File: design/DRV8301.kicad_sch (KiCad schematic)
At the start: 38 parts, among them U2 LM3671, U3 DRV8301

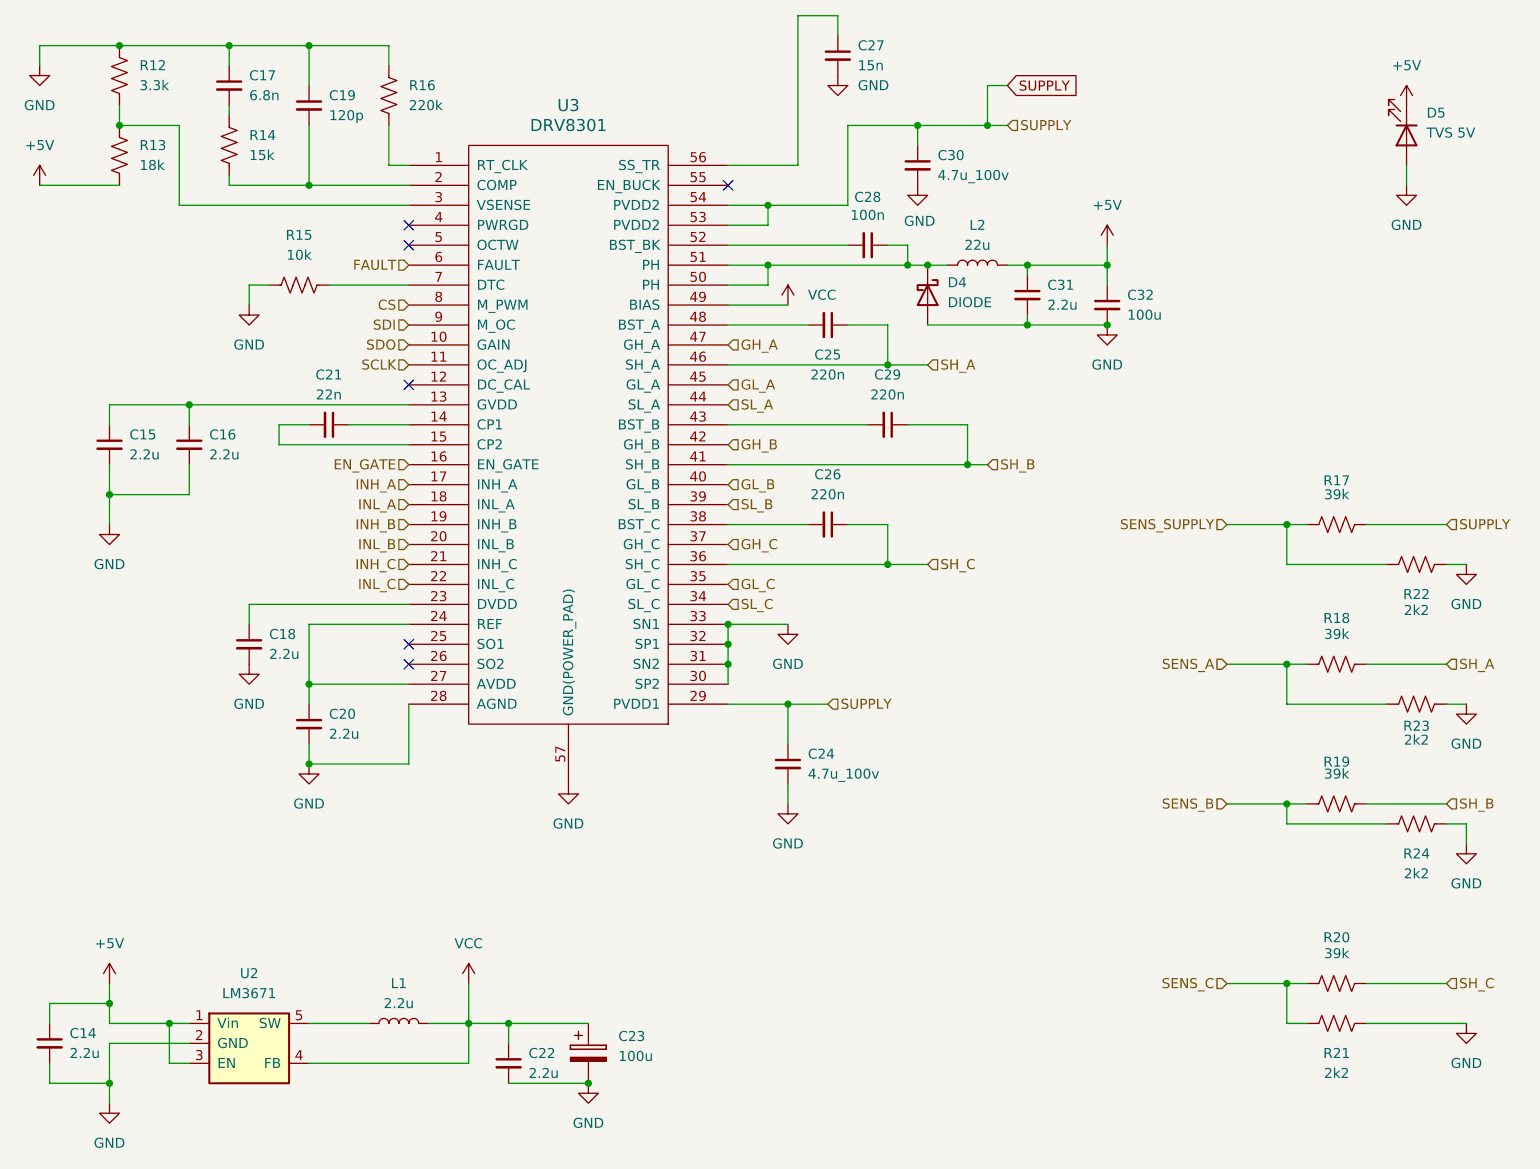
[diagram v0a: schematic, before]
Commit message: Impresión de esquemático en pdf
Impresión de la versión del esquemático en la carpeta /pdf
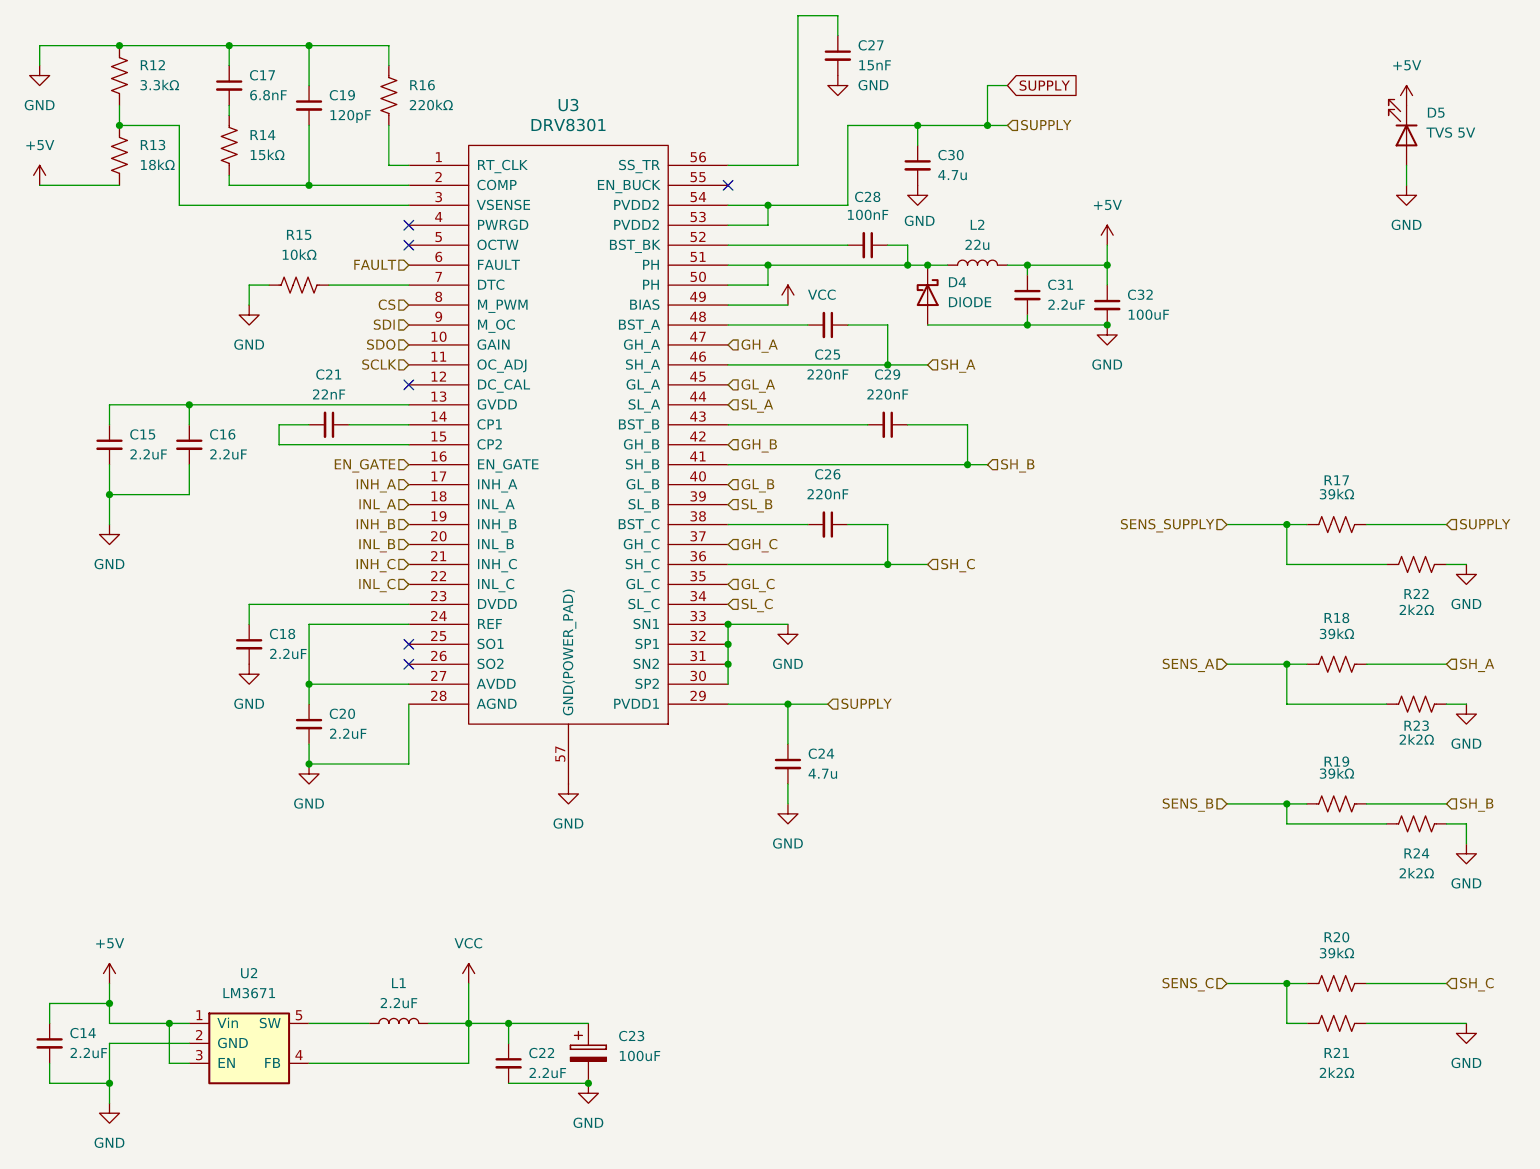
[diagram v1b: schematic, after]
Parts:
- C14, C15, C16, C18, C20, C22, C31, L1: value 2.2u -> 2.2uF
- C17: value 6.8n -> 6.8nF; footprint Capacitor_SMD:C_0603_1608Metric -> Capacitor_SMD:C_1206_3216Metric
- C19: value 120p -> 120pF
- C21: value 22n -> 22nF
- C23, C32: value 100u -> 100uF; footprint Capacitor_SMD:C_0603_1608Metric -> Capacitor_SMD:C_1206_3216Metric
- C24, C30: value 4.7u_100v -> 4.7u; footprint Capacitor_SMD:C_0603_1608Metric -> Capacitor_SMD:C_1210_3225Metric
- C25, C26, C29: value 220n -> 220nF
- C27: value 15n -> 15nF
- C28: value 100n -> 100nF
- R12: value 3.3k -> 3.3kΩ
- R13: value 18k -> 18kΩ
- R14: value 15k -> 15kΩ
- R15: value 10k -> 10kΩ
- R16: value 220k -> 220kΩ
- R17, R18, R19, R20: value 39k -> 39kΩ
- R21, R22, R23, R24: value 2k2 -> 2k2Ω
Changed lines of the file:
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@@
 			)
 		)
-		(property "Value" "220k"
+		(property "Value" "220kΩ"
 			(at 121.92 30.4799 0)
 			(effects
@@
 			)
 		)
-		(property "Value" "18k"
+		(property "Value" "18kΩ"
 			(at 87.63 38.0999 0)
 			(effects
@@
 			)
 		)
-		(property "Value" "3.3k"
+		(property "Value" "3.3kΩ"
 			(at 87.63 27.9399 0)
 			(effects
@@
 			)
 		)
-		(property "Value" "15k"
+		(property "Value" "15kΩ"
 			(at 101.6 36.8299 0)
 			(effects
@@
 			)
 		)
-		(property "Value" "6.8n"
+		(property "Value" "6.8nF"
 			(at 101.6 29.2162 0)
 			(effects
@@
 			)
 		)
-		(property "Footprint" "Capacitor_SMD:C_0603_1608Metric"
+		(property "Footprint" "Capacitor_SMD:C_1206_3216Metric"
 			(at 99.06 27.94 0)
 			(effects
@@
 			)
 		)
-		(property "Description" ""
+		(property "Description" "CAP CER 6.8NF 1206"
 			(at 99.06 27.94 0)
 			(effects
@@
 			)
 		)
-		(property "Value" "120p"
+		(property "Value" "120pF"
 			(at 111.76 31.7562 0)
 			(effects
@@
 			)
 		)
-		(property "Description" ""
+		(property "Description" "CAP CER 120PF 0603"
 			(at 109.22 30.48 0)
 			(effects
@@
 			)
 		)
-		(property "Value" "22n"
+		(property "Value" "22nF"
 			(at 111.7536 67.31 90)
 			(effects
@@
 			)
 		)
-		(property "Description" ""
+		(property "Description" "CAP CER 22NF 0603"
 			(at 111.76 71.12 0)
 			(effects
@@
 			)
 		)
-		(property "Value" "2.2u"
+		(property "Value" "2.2uF"
 			(at 96.52 74.9362 0)
 			(effects
@@
 			)
 		)
-		(property "Value" "2.2u"
+		(property "Value" "2.2uF"
 			(at 86.36 74.9362 0)
 			(effects
@@
 			)
 		)
-		(property "Value" "2.2u"
+		(property "Value" "2.2uF"
 			(at 104.14 100.3362 0)
 			(effects
@@
 			)
 		)
-		(property "Value" "2.2u"
+		(property "Value" "2.2uF"
 			(at 111.76 110.4962 0)
 			(effects
@@
 			)
 		)
-		(property "Value" "15n"
+		(property "Value" "15nF"
 			(at 179.07 25.4062 0)
 			(effects
@@
 			)
 		)
-		(property "Description" ""
+		(property "Description" "CAP CER 0603 15nF 16V X7R 10%"
 			(at 176.53 24.13 0)
 			(effects
@@
 			)
 		)
-		(property "Value" "4.7u_100v"
+		(property "Value" "4.7u"
 			(at 189.23 39.3762 0)
 			(effects
@@
 			)
 		)
-		(property "Footprint" "Capacitor_SMD:C_0603_1608Metric"
+		(property "Footprint" "Capacitor_SMD:C_1210_3225Metric"
 			(at 186.69 38.1 0)
 			(effects
@@
 			)
 		)
-		(property "Description" ""
+		(property "Description" "CAP CER 4.7UF 100V X7R 1210"
 			(at 186.69 38.1 0)
 			(effects
@@
 			)
 		)
-		(property "Value" "220n"
+		(property "Value" "220nF"
 			(at 175.2536 64.77 90)
 			(effects
@@
 			)
 		)
-		(property "Description" ""
+		(property "Description" "CAP CER 0603 220nF 25V X7R 10%"
 			(at 175.26 58.42 0)
 			(effects
@@
 			)
 		)
-		(property "Value" "100n"
+		(property "Value" "100nF"
 			(at 180.3336 44.45 90)
 			(effects
@@
 			)
 		)
-		(property "Value" "220n"
+		(property "Value" "220nF"
 			(at 182.8736 67.31 90)
 			(effects
@@
 			)
 		)
-		(property "Description" ""
+		(property "Description" "CAP CER 0603 220nF 25V X7R 10%"
 			(at 182.88 71.12 0)
 			(effects
@@
 			)
 		)
-		(property "Value" "220n"
+		(property "Value" "220nF"
 			(at 175.2536 80.01 90)
 			(effects
@@
 			)
 		)
-		(property "Description" ""
+		(property "Description" "CAP CER 0603 220nF 25V X7R 10%"
 			(at 175.26 83.82 0)
 			(effects
@@
 			)
 		)
-		(property "Value" "2.2u"
+		(property "Value" "2.2uF"
 			(at 203.2 55.8862 0)
 			(effects
@@
 			)
 		)
-		(property "Value" "100u"
+		(property "Value" "100uF"
 			(at 213.36 57.1562 0)
 			(effects
@@
 			)
 		)
-		(property "Footprint" "Capacitor_SMD:C_0603_1608Metric"
+		(property "Footprint" "Capacitor_SMD:C_1206_3216Metric"
 			(at 210.82 55.88 0)
 			(effects
@@
 			)
 		)
-		(property "Description" ""
+		(property "Description" "CAP CER 100UF 1206"
 			(at 210.82 55.88 0)
 			(effects
@@
 			)
 		)
-		(property "Value" "4.7u_100v"
+		(property "Value" "4.7u"
 			(at 172.72 115.5762 0)
 			(effects
@@
 			)
 		)
-		(property "Footprint" "Capacitor_SMD:C_0603_1608Metric"
+		(property "Footprint" "Capacitor_SMD:C_1210_3225Metric"
 			(at 170.18 114.3 0)
 			(effects
@@
 			)
 		)
-		(property "Description" ""
+		(property "Description" "CAP CER 4.7UF 100V X7R 1210"
 			(at 170.18 114.3 0)
 			(effects
@@
 			)
 		)
-		(property "Value" "39k"
+		(property "Value" "39kΩ"
 			(at 240.03 80.01 90)
 			(effects
@@
 			)
 		)
-		(property "Value" "2k2"
+		(property "Value" "2k2Ω"
 			(at 250.19 94.742 90)
 			(effects
@@
 			)
 		)
-		(property "Value" "39k"
+		(property "Value" "39kΩ"
 			(at 240.03 97.79 90)
 			(effects
@@
 			)
 		)
-		(property "Value" "2k2"
+		(property "Value" "2k2Ω"
 			(at 250.19 111.252 90)
 			(effects
@@
 			)
 		)
-		(property "Value" "39k"
+		(property "Value" "39kΩ"
 			(at 240.03 115.57 90)
 			(effects
@@
 			)
 		)
-		(property "Value" "2k2"
+		(property "Value" "2k2Ω"
 			(at 250.19 128.27 90)
 			(effects
@@
 			)
 		)
-		(property "Value" "39k"
+		(property "Value" "39kΩ"
 			(at 240.03 138.43 90)
 			(effects
@@
 			)
 		)
-		(property "Value" "2k2"
+		(property "Value" "2k2Ω"
 			(at 240.03 153.67 90)
 			(effects
@@
 			)
 		)
-		(property "Value" "10k"
+		(property "Value" "10kΩ"
 			(at 107.95 49.53 90)
 			(effects
@@
 			)
 		)
-		(property "Value" "2.2u"
+		(property "Value" "2.2uF"
 			(at 120.65 144.78 90)
 			(effects
@@
 			)
 		)
-		(property "Value" "2.2u"
+		(property "Value" "2.2uF"
 			(at 137.16 153.6762 0)
 			(effects
@@
 			)
 		)
-		(property "Value" "2.2u"
+		(property "Value" "2.2uF"
 			(at 78.74 151.1362 0)
 			(effects
@@
 			)
 		)
-		(property "Value" "100u"
+		(property "Value" "100uF"
 			(at 148.59 151.5109 0)
 			(effects
@@
 			)
 		)
-		(property "Footprint" "Capacitor_SMD:C_0603_1608Metric"
+		(property "Footprint" "Capacitor_SMD:C_1206_3216Metric"
 			(at 145.7452 154.94 0)
 			(effects
@@
 			)
 		)
-		(property "Description" ""
+		(property "Description" "CAP CER 100UF 1206"
 			(at 144.78 151.13 0)
 			(effects

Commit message: Agregado de footprints
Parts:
- D4: footprint (none) -> Diode_SMD:D_SMA
- D5: footprint (none) -> LED_SMD:LED_0603_1608Metric
- L2: footprint (none) -> Inductor_SMD:L_0603_1608Metric_Pad1.05x0.95mm_HandSolder
- U2: footprint (none) -> crf1:MF05A
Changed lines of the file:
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@@
 			)
 		)
-		(property "Footprint" ""
+		(property "Footprint" "LED_SMD:LED_0603_1608Metric"
 			(at 248.92 34.29 0)
 			(effects
@@
 			)
 		)
-		(property "Description" ""
+		(property "Description" "LED"
 			(at 248.92 34.29 0)
 			(effects
@@
 			)
 		)
-		(property "Description" "R 2k2, 0603 "
+		(property "Description" "R 2k2, 0603"
 			(at 250.19 88.9 0)
 			(effects
@@
 			)
 		)
-		(property "Description" "R 2k2, 0603 "
+		(property "Description" "R 2k2, 0603"
 			(at 250.19 106.68 0)
 			(effects
@@
 			)
 		)
-		(property "Description" "R 2k2, 0603 "
+		(property "Description" "R 2k2, 0603"
 			(at 250.19 121.92 0)
 			(effects
@@
 			)
 		)
-		(property "Description" "R 2k2, 0603 "
+		(property "Description" "R 2k2, 0603"
 			(at 240.03 147.32 0)
 			(effects
@@
 			)
 		)
-		(property "Footprint" ""
+		(property "Footprint" "Diode_SMD:D_SMA"
 			(at 187.96 54.61 0)
 			(effects
@@
 			)
 		)
-		(property "Description" "Shottky 60V 2A "
+		(property "Description" "Shottky 60V 2A"
 			(at 187.96 54.61 0)
 			(effects
@@
 			)
 		)
-		(property "Footprint" ""
+		(property "Footprint" "Inductor_SMD:L_0603_1608Metric_Pad1.05x0.95mm_HandSolder"
 			(at 194.31 50.8 0)
 			(effects
@@
 			)
 		)
-		(property "Footprint" ""
+		(property "Footprint" "crf1:MF05A"
 			(at 101.6 149.86 0)
 			(effects

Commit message: Agrego MFR.Part # a capacitores
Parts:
- C14, C15, C16, C18, C20, C22, C31, L1: Manufacturer (none) -> Samsung Electro-Mechanics; Manufacturer Product Number  (none) -> CL10A225KO8NNNC
- C28: Manufacturer (none) -> YAGEO; Manufacturer Product Number  (none) -> CC0603KRX7R9BB104
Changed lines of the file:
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@@
+			)
+		)
+		(property "Manufacturer" "Samsung Electro-Mechanics"
+			(at 93.98 73.66 0)
+			(effects
+				(font
+					(size 1.27 1.27)
+				)
+				(hide yes)
+			)
+		)
+		(property "Manufacturer Product Number " "CL10A225KO8NNNC"
+			(at 93.98 73.66 0)
+			(effects
+				(font
+					(size 1.27 1.27)
+				)
+				(hide yes)
 			)
 		)
@@
 			)
 		)
+		(property "Manufacturer" "Samsung Electro-Mechanics"
+			(at 83.82 73.66 0)
+			(effects
+				(font
+					(size 1.27 1.27)
+				)
+				(hide yes)
+			)
+		)
+		(property "Manufacturer Product Number " "CL10A225KO8NNNC"
+			(at 83.82 73.66 0)
+			(effects
+				(font
+					(size 1.27 1.27)
+				)
+				(hide yes)
+			)
+		)
 		(pin "2"
 		)
@@
 			)
 		)
+		(property "Manufacturer" "Samsung Electro-Mechanics"
+			(at 101.6 99.06 0)
+			(effects
+				(font
+					(size 1.27 1.27)
+				)
+				(hide yes)
+			)
+		)
+		(property "Manufacturer Product Number " "CL10A225KO8NNNC"
+			(at 101.6 99.06 0)
+			(effects
+				(font
+					(size 1.27 1.27)
+				)
+				(hide yes)
+			)
+		)
 		(pin "1"
 		)
@@
 			)
 		)
+		(property "Manufacturer" "Samsung Electro-Mechanics"
+			(at 109.22 109.22 0)
+			(effects
+				(font
+					(size 1.27 1.27)
+				)
+				(hide yes)
+			)
+		)
+		(property "Manufacturer Product Number " "CL10A225KO8NNNC"
+			(at 109.22 109.22 0)
+			(effects
+				(font
+					(size 1.27 1.27)
+				)
+				(hide yes)
+			)
+		)
 		(pin "1"
 		)
@@
 			)
 		)
+		(property "Manufacturer" "YAGEO"
+			(at 180.34 48.26 0)
+			(effects
+				(font
+					(size 1.27 1.27)
+				)
+				(hide yes)
+			)
+		)
+		(property "Manufacturer Product Number " "CC0603KRX7R9BB104"
+			(at 180.34 48.26 0)
+			(effects
+				(font
+					(size 1.27 1.27)
+				)
+				(hide yes)
+			)
+		)
 		(pin "1"
 		)
@@
 			)
 		)
+		(property "Manufacturer" "Samsung Electro-Mechanics"
+			(at 200.66 54.61 0)
+			(effects
+				(font
+					(size 1.27 1.27)
+				)
+				(hide yes)
+			)
+		)
+		(property "Manufacturer Product Number " "CL10A225KO8NNNC"
+			(at 200.66 54.61 0)
+			(effects
+				(font
+					(size 1.27 1.27)
+				)
+				(hide yes)
+			)
+		)
 		(pin "1"
 		)
@@
 			)
 		)
+		(property "Manufacturer" "Samsung Electro-Mechanics"
+			(at 120.65 147.32 0)
+			(effects
+				(font
+					(size 1.27 1.27)
+				)
+				(hide yes)
+			)
+		)
+		(property "Manufacturer Product Number " "CL10A225KO8NNNC"
+			(at 120.65 147.32 0)
+			(effects
+				(font
+					(size 1.27 1.27)
+				)
+				(hide yes)
+			)
+		)
 		(pin "2"
 		)
@@
 			)
 		)
+		(property "Manufacturer" "Samsung Electro-Mechanics"
+			(at 134.62 152.4 0)
+			(effects
+				(font
+					(size 1.27 1.27)
+				)
+				(hide yes)
+			)
+		)
+		(property "Manufacturer Product Number " "CL10A225KO8NNNC"
+			(at 134.62 152.4 0)
+			(effects
+				(font
+					(size 1.27 1.27)
+				)
+				(hide yes)
+			)
+		)
 		(pin "1"
 		)
@@
 			(at 76.2 149.86 0)
 			(effects
+				(font
+					(size 1.27 1.27)
+				)
+				(hide yes)
+			)
+		)
+		(property "Manufacturer" "Samsung Electro-Mechanics"
+			(at 76.2 149.86 0)
+			(effects
+				(font
+					(size 1.27 1.27)
+				)
+				(hide yes)
+			)
+		)
+		(property "Manufacturer Product Number " "CL10A225KO8NNNC"
+			(at 76.2 149.86 0)
+			(effects

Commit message: Agregue Manufacturer Product Numbers
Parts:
- C17: Manufacturer (none) -> YAGEO; Manufacturer Product Number  (none) -> CC1206KKX7RCBB682
- C19: Manufacturer (none) -> YAGEO; Manufacturer Product Number  (none) -> CC0603JRNPOYBN121
- C21: Manufacturer (none) -> Samsung Electro-Mechanics; Manufacturer Product Number  (none) -> CL10B223KC8WPNC
- C23, C32: Manufacturer (none) -> Samsung Electro-Mechanics; Manufacturer Product Number  (none) -> CL31A107MQHNNNE
- C24, C30: Manufacturer (none) -> Holy Stone Enterprise Co., Ltd.; Manufacturer Product Number  (none) -> C1210X475K101T
- C25, C26, C29: Manufacturer (none) -> Samsung Electro-Mechanics; Manufacturer Product Number  (none) -> CL10B224KA8NNNC
- C27: Manufacturer (none) -> YAGEO; Manufacturer Product Number  (none) -> CC0603KRX7R8BB153
- D4: Manufacturer (none) -> FUXINSEMI; Manufacturer Product Number  (none) -> B260A
- D5: Manufacturer (none) -> ROHM Semicon; Manufacturer Product Number  (none) -> SML-310VTT86
- L2: Manufacturer (none) -> Murata Electronics; Manufacturer Product Number  (none) -> LQM18DN220M70L
- R12: Manufacturer (none) -> YAGEO; Manufacturer Product Number  (none) -> RC0603FR-073K3L
- R13: Manufacturer (none) -> YAGEO; Manufacturer Product Number  (none) -> RT0603BRD0718KL
- R14: Manufacturer (none) -> YAGEO; Manufacturer Product Number  (none) -> RC0603FR-0715KL
- R15: Manufacturer (none) -> YAGEO; Manufacturer Product Number  (none) -> RC0603FR-0710KL
- R16: Manufacturer (none) -> YAGEO; Manufacturer Product Number  (none) -> RC0603FR-07220KL
- R17, R18, R19, R20: Manufacturer (none) -> YAGEO; Manufacturer Product Number  (none) -> RC0603FR-0739KL
- R21, R22, R23, R24: Manufacturer (none) -> YAGEO; Manufacturer Product Number  (none) -> AC0603DR-072K2L
- U2: Manufacturer (none) -> Texas Instruments; Manufacturer Product Number  (none) -> LM3671MF-1.2/NOPB
- U3: Manufacturer (none) -> Texas Instruments; Manufacturer Product Number  (none) -> DRV8301DCAR

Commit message: Agregue Manufacturer Product Number
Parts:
- removed C14: 2.2uF, Capacitor_SMD:C_0603_1608Metric, symbol Device:C_Small
- added C13: 4.7u, Capacitor_SMD:C_1210_3225Metric, symbol Device:C_Small
- renumbered C15 to C14, C16 to C15, C17 to C16, C18 to C17, C19 to C18, C20 to C19, C21 to C20, C22 to C21, C23 to C22, C24 to C23, C25 to C24, C26 to C25, C27 to C26, C28 to C27, C29 to C28, C30 to C29, C31 to C30, C32 to C31, R12 to R14, R13 to R15, R14 to R16, R15 to R17, R16 to R18, R17 to R19, R18 to R20, R19 to R21, R20 to R22, R21 to R23, R22 to R24, R23 to R25, R24 to R26
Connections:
- net +5V: now also C13.1
- net GND: now also C13.2
